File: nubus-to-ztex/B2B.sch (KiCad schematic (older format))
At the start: 13 parts, among them J1 87832-1420 (2x7 M 2mm), J3 Conn_01x06_Male

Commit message: update
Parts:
- J1: DNP DNP -> (none)
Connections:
- net ~ID3_3V3 is gone; now on net ~RESET_3V3: JCD1.7 (U8~IO_25_34)
- net ~RESET_3V3: no longer JCD1.30 (R3~IO_L11P_T1_SRCC_34)
- new net CLK_54_000: JCD1.30 (R3~IO_L11P_T1_SRCC_34)
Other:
- note added: "The two LED signals are also\nconnected to the serial connector\nfor debugging purposes"
- note removed: "The four LED signals are also\nconnected to the serial connector\nfor debugging purposes"
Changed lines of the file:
@@
 $Descr A4 11693 8268
 encoding utf-8
-Sheet 2 8
+Sheet 2 9
 Title "nubus-to-ztex B2B connector"
 Date ""
@@
 F 4 "87832-1420" H 3150 7250 50  0001 C CNN "MPN"
 F 5 "https://www.mouser.fr/ProductDetail/Molex/87832-1420?qs=9Wl4wMk6Njp2JciwISLQUQ%3D%3D" H 3150 7250 50  0001 C CNN "URL"
-F 6 "DNP" H 3150 7250 50  0000 C CNN "DNP"
 	1    3150 7250
 	1    0    0    -1
@@
 Text GLabel 4100 2150 2    50   Input ~ 0
 ~AD30_3V3
-Text GLabel 9900 2550 2    50   Input ~ 0
+Text GLabel 7400 1450 0    50   Input ~ 0
 ~RESET_3V3
 Text GLabel 7400 2350 0    50   Input ~ 0
@@
 Text GLabel 7400 1550 0    50   Input ~ 0
 ~ID0_3V3
-Text GLabel 7400 1450 0    50   Input ~ 0
-~ID3_3V3
 Text GLabel 7400 3450 0    50   Input ~ 0
 HDMI_CLK+
@@
 Molex 10-89-7642 a.k.a. A-70280-0072, with dimension 11.1 (total), 6.1 (mating) & 2.72 (solder), Hole diameter 1.02\nXKB X6521WV-2x32H-C30D60 is 11.5/6/3, H1.02\nAmphenol 77313-824-64LF is 12.2/6.75/2.9, H1.02\nAmphenol 77313-818-64LF is 11.43/5.84/3.05, H1.02\nAmphenol 77313-101-64LF is 10.8/5.84/2.41, H1.02 ('1xx' has thicker gold coating than '8xx')\nWurth 61306421121 is 11.54/6/3, H1.10\n
 Text Notes 2450 6750 1    50   ~ 0
-The four LED signals are also\nconnected to the serial connector\nfor debugging purposes
+The two LED signals are also\nconnected to the serial connector\nfor debugging purposes
 Connection ~ 6250 2550
 Text GLabel 9900 3250 2    50   Input ~ 0
@@
 Wire Wire Line
 	10575 1100 10775 1100
+Text GLabel 9900 2550 2    50   Input Italic 0
+CLK_54_000
 $EndSCHEMATC

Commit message: some BoM optimization
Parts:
- C1, C2: MPN CC0603KRX7R8BB104 -> CC0603KRX7R9BB104; URL https://www.lcsc.com/product-detail/Multilayer-Ceramic-Capacitors-MLCC-SMD-SMT_YAGEO-CC0603KRX7R8BB104_C92490.html -> https://www.lcsc.com/product-detail/Multilayer-Ceramic-Capacitors-MLCC-SMD-SMT_YAGEO-CC0603KRX7R9BB104_C14663.html
- D1, D2: value RED Led 0805 -> RED Led 0603; footprint LED_SMD:LED_0805_2012Metric -> LED_SMD:LED_0603_1608Metric; MNF1_URL www.liteon.com -> (none); MPN LTST-C170KRKT -> 19-217/R6C-AL1M2VY/3T; URL https://www.lcsc.com/product-detail/Light-Emitting-Diodes-LED_Lite-On-LTST-C170KRKT_C94868.html -> https://www.lcsc.com/product-detail/Light-Emitting-Diodes-LED_Everlight-Elec-19-217-R6C-AL1M2VY-3T_C72044.html
- D3: value BLUE Led 0805 -> BLUE Led 0603; footprint LED_SMD:LED_0805_2012Metric -> LED_SMD:LED_0603_1608Metric; MNF1_URL www.liteon.com -> (none); MPN LTST-C170TBKT -> 19-217/BHC-ZL1M2RY/3T; URL https://www.lcsc.com/product-detail/Light-Emitting-Diodes-LED_LTST-C170TBKT-blue_C98222.html -> https://www.lcsc.com/product-detail/Light-Emitting-Diodes-LED_Everlight-Elec-19-217-BHC-ZL1M2RY-3T_C72041.html
- J1: value 87832-1420 (2x7 M 2mm) -> 87831-1420 (2x7 M 2mm); footprint For_SeeedStudio:MOLEX_87832-1420 -> For_SeeedStudio:PinHeader_2x07_P2.00mm_Vertical_For_SeeedStudio; MPN 87832-1420 -> 87831-1420; URL https://www.mouser.fr/ProductDetail/Molex/87832-1420?qs=9Wl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 -> https://www.mouser.fr/ProductDetail/Molex/87831-1420?qs=QtQ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
- JAB1, JCD1: MPN 10-89-7642 -> X6521WV-2x32H-C30D60; URL https://www.mouser.fr/ProductDetail/Molex/10-89-7642?qs=oWQ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 -> https://www.lcsc.com/product-detail/Pin-Headers_XKB-Connect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; URL (Molex) https://www2.mouser.com/ProductDetail/Molex/10-89-7642?qs=%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 -> https://www.mouser.fr/ProductDetail/Molex/10-89-7642?qs=oWQ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
- R1, R2, R3: value 590 -> 560; MPN 0603WAF5900T5E -> 0603WAF5600T5E; URL https://www.lcsc.com/product-detail/Chip-Resistor-Surface-Mount_UNI-ROYAL-Uniroyal-Elec-0603WAF5900T5E_C23084.html -> https://www.lcsc.com/product-detail/Chip-Resistor-Surface-Mount_UNI-ROYAL-Uniroyal-Elec-0603WAF5600T5E_C23204.html
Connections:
- net PMOD-10 renamed PMOD-910+
- net PMOD-11 renamed PMOD-1112-
- net PMOD-12 renamed PMOD-1112+
- net PMOD-13 renamed PMOD-1314-
- net PMOD-14 renamed PMOD-1314+
- net PMOD-15 renamed PMOD-1516-
- net PMOD-16 renamed PMOD-1516+
- net PMOD-5 renamed PMOD-56-
- net PMOD-6 renamed PMOD-56+
- net PMOD-7 renamed PMOD-78-
- net PMOD-8 renamed PMOD-78+
- net PMOD-9 renamed PMOD-910-

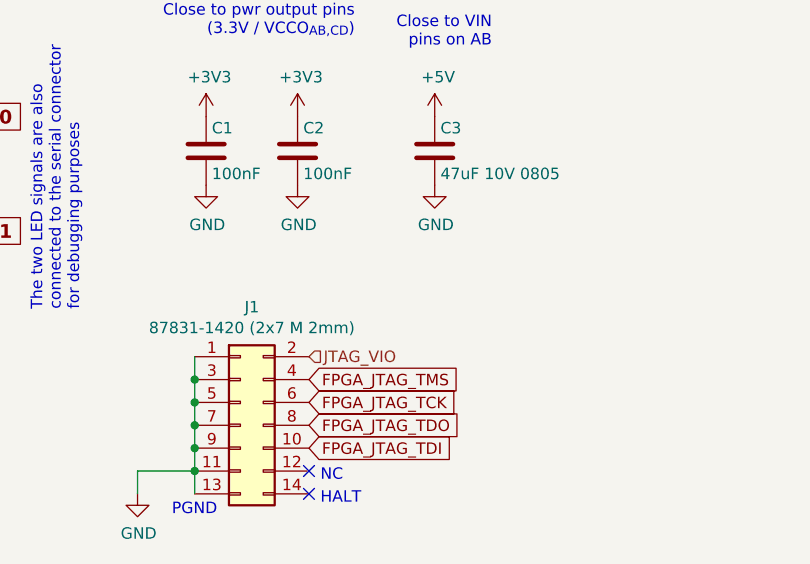
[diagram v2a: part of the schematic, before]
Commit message: even more JLCPCB BoM optimization
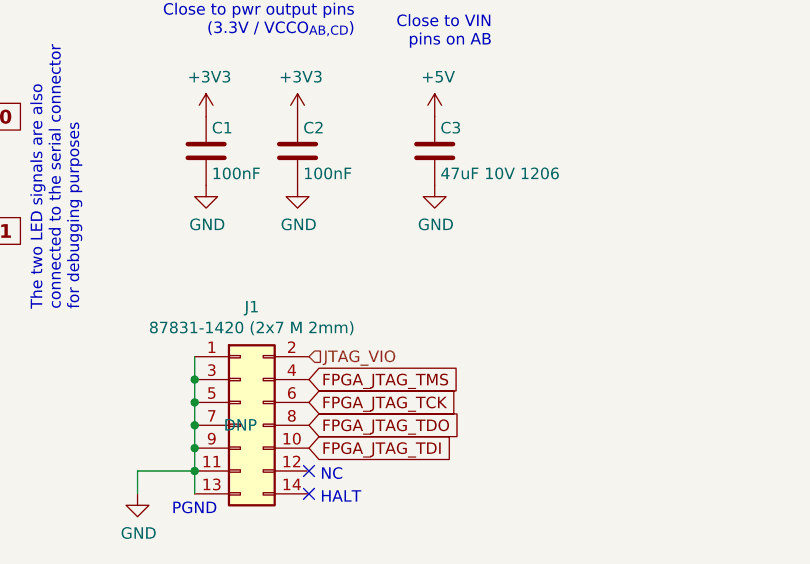
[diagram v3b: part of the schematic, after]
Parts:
- C3: value 47uF 10V 0805 -> 47uF 10V 1206; footprint Capacitor_SMD:C_0805_2012Metric -> Capacitor_SMD:C_1206_3216Metric; MPN C2012X5R1A476MTJ00E -> CL31A476MPHNNNE; URL https://www.lcsc.com/product-detail/Multilayer-Ceramic-Capacitors-MLCC-SMD-SMT_TDK-C2012X5R1A476MTJ00E_C76636.html -> https://www.lcsc.com/product-detail/Multilayer-Ceramic-Capacitors-MLCC-SMD-SMT_Samsung-Electro-Mechanics-CL31A476MPHNNNE_C96123.html
- D1, D2: MPN 19-217/R6C-AL1M2VY/3T -> KT-0603R; URL https://www.lcsc.com/product-detail/Light-Emitting-Diodes-L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 -> https://jlcpcb.com/partdetail/Hubei_KentoElec-KT0603R/C2286
- J1: DNP (none) -> DNP
- JAB1, JCD1: MPN X6521WV-2x32H-C30D60 -> 77313-824-64LF; URL https://www.lcsc.com/product-detail/Pin-Headers_XKB-Connect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 -> https://eu.mouser.com/ProductDetail/Amphenol-FCI/77313-101-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
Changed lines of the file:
@@
 F 8 "77313-101-64LF" H 1800 2650 50  0001 C CNN "MPN (Amphenol)"
 F 9 "https://eu.mouser.com/ProductDetail/Amphenol-FCI/77313-101-64LF?qs=xJiur%252Bgubk1MSan%2F7C0v%252BA%3D%3D" H 1800 2650 50  0001 C CNN "URL (Amphenol)"
-F 10 "X6521WV-2x32H-C30D60" H 1800 2650 50  0001 C CNN "MPN"
-F 11 "https://www.lcsc.com/product-detail/Pin-Headers_XKB-Connectivity-X6521WV-2x32H-C30D60_C2883966.html" H 1800 2650 50  0001 C CNN "URL"
+F 10 "77313-824-64LF" H 1800 2650 50  0001 C CNN "MPN"
+F 11 "https://eu.mouser.com/ProductDetail/Amphenol-FCI/77313-101-64LF?qs=xJiur%252Bgubk1MSan%2F7C0v%252BA%3D%3D" H 1800 2650 50  0001 C CNN "URL"
 	1    1800 2650
 	1    0    0    -1
@@
 F 8 "77313-101-64LF" H 1800 2650 50  0001 C CNN "MPN (Amphenol)"
 F 9 "https://eu.mouser.com/ProductDetail/Amphenol-FCI/77313-101-64LF?qs=xJiur%252Bgubk1MSan%2F7C0v%252BA%3D%3D" H 1800 2650 50  0001 C CNN "URL (Amphenol)"
-F 10 "X6521WV-2x32H-C30D60" H 7600 2650 50  0001 C CNN "MPN"
-F 11 "https://www.lcsc.com/product-detail/Pin-Headers_XKB-Connectivity-X6521WV-2x32H-C30D60_C2883966.html" H 7600 2650 50  0001 C CNN "URL"
+F 10 "77313-824-64LF" H 7600 2650 50  0001 C CNN "MPN"
+F 11 "https://eu.mouser.com/ProductDetail/Amphenol-FCI/77313-101-64LF?qs=xJiur%252Bgubk1MSan%2F7C0v%252BA%3D%3D" H 7600 2650 50  0001 C CNN "URL"
 	1    7600 2650
 	1    0    0    -1
@@
 F 4 "87831-1420" H 3150 7250 50  0001 C CNN "MPN"
 F 5 "https://www.mouser.fr/ProductDetail/Molex/87831-1420?qs=QtQX4uD3c2VDCL534TqpVg%3D%3D" H 3150 7250 50  0001 C CNN "URL"
+F 6 "DNP" H 3150 7250 50  0000 C CNN "DNP"
 	1    3150 7250
 	1    0    0    -1
@@
 F 3 "https://optoelectronics.liteon.com/upload/download/DS-22-99-0150/LTST-C170KRKT.pdf" H 1000 5900 50  0001 C CNN
 F 4 "" H 1000 5900 60  0001 C CNN "MNF1_URL"
-F 5 "19-217/R6C-AL1M2VY/3T" H 1000 5900 60  0001 C CNN "MPN"
-F 6 "https://www.lcsc.com/product-detail/Light-Emitting-Diodes-LED_Everlight-Elec-19-217-R6C-AL1M2VY-3T_C72044.html" H 1000 5900 50  0001 C CNN "URL"
+F 5 "KT-0603R" H 1000 5900 60  0001 C CNN "MPN"
+F 6 "https://jlcpcb.com/partdetail/Hubei_KentoElec-KT0603R/C2286" H 1000 5900 50  0001 C CNN "URL"
 	1    1000 5900
 	1    0    0    -1
@@
 F 3 "https://optoelectronics.liteon.com/upload/download/DS-22-99-0150/LTST-C170KRKT.pdf" H 1000 6400 50  0001 C CNN
 F 4 "" H 1000 6400 60  0001 C CNN "MNF1_URL"
-F 5 "19-217/R6C-AL1M2VY/3T" H 1000 6400 60  0001 C CNN "MPN"
-F 6 "https://www.lcsc.com/product-detail/Light-Emitting-Diodes-LED_Everlight-Elec-19-217-R6C-AL1M2VY-3T_C72044.html" H 1000 6400 50  0001 C CNN "URL"
+F 5 "KT-0603R" H 1000 6400 60  0001 C CNN "MPN"
+F 6 "https://jlcpcb.com/partdetail/Hubei_KentoElec-KT0603R/C2286" H 1000 6400 50  0001 C CNN "URL"
 	1    1000 6400
 	1    0    0    -1
@@
 AR Path="/618E8C75/621FCA7B" Ref="C3"  Part="1"
 F 0 "C3" H 4025 6150 50  0000 L CNN
-F 1 "47uF 10V 0805" H 4025 5950 50  0000 L CNN
-F 2 "Capacitor_SMD:C_0805_2012Metric" H 4038 5900 50  0001 C CNN
+F 1 "47uF 10V 1206" H 4025 5950 50  0000 L CNN
+F 2 "Capacitor_SMD:C_1206_3216Metric" H 4038 5900 50  0001 C CNN
 F 3 "" H 4000 6050 50  0000 C CNN
 F 4 "C2012X5R1A476MTJ00E" H 4000 6050 50  0001 C CNN "MPN-ALT"
 F 5 "https://lcsc.com/product-detail/Multilayer-Ceramic-Capacitors-MLCC-SMD-SMT_TDK-C2012X5R1A476MTJ00E_C76636.html" H 4000 6050 50  0001 C CNN "URL-ALT"
-F 6 "C2012X5R1A476MTJ00E" H 4000 6050 50  0001 C CNN "MPN"
-F 7 "https://www.lcsc.com/product-detail/Multilayer-Ceramic-Capacitors-MLCC-SMD-SMT_TDK-C2012X5R1A476MTJ00E_C76636.html" H 4000 6050 50  0001 C CNN "URL"
+F 6 "CL31A476MPHNNNE" H 4000 6050 50  0001 C CNN "MPN"
+F 7 "https://www.lcsc.com/product-detail/Multilayer-Ceramic-Capacitors-MLCC-SMD-SMT_Samsung-Electro-Mechanics-CL31A476MPHNNNE_C96123.html" H 4000 6050 50  0001 C CNN "URL"
 	1    4000 6050
 	1    0    0    -1
